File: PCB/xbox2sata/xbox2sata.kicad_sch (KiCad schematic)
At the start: 3 parts, among them U1 88SA8052

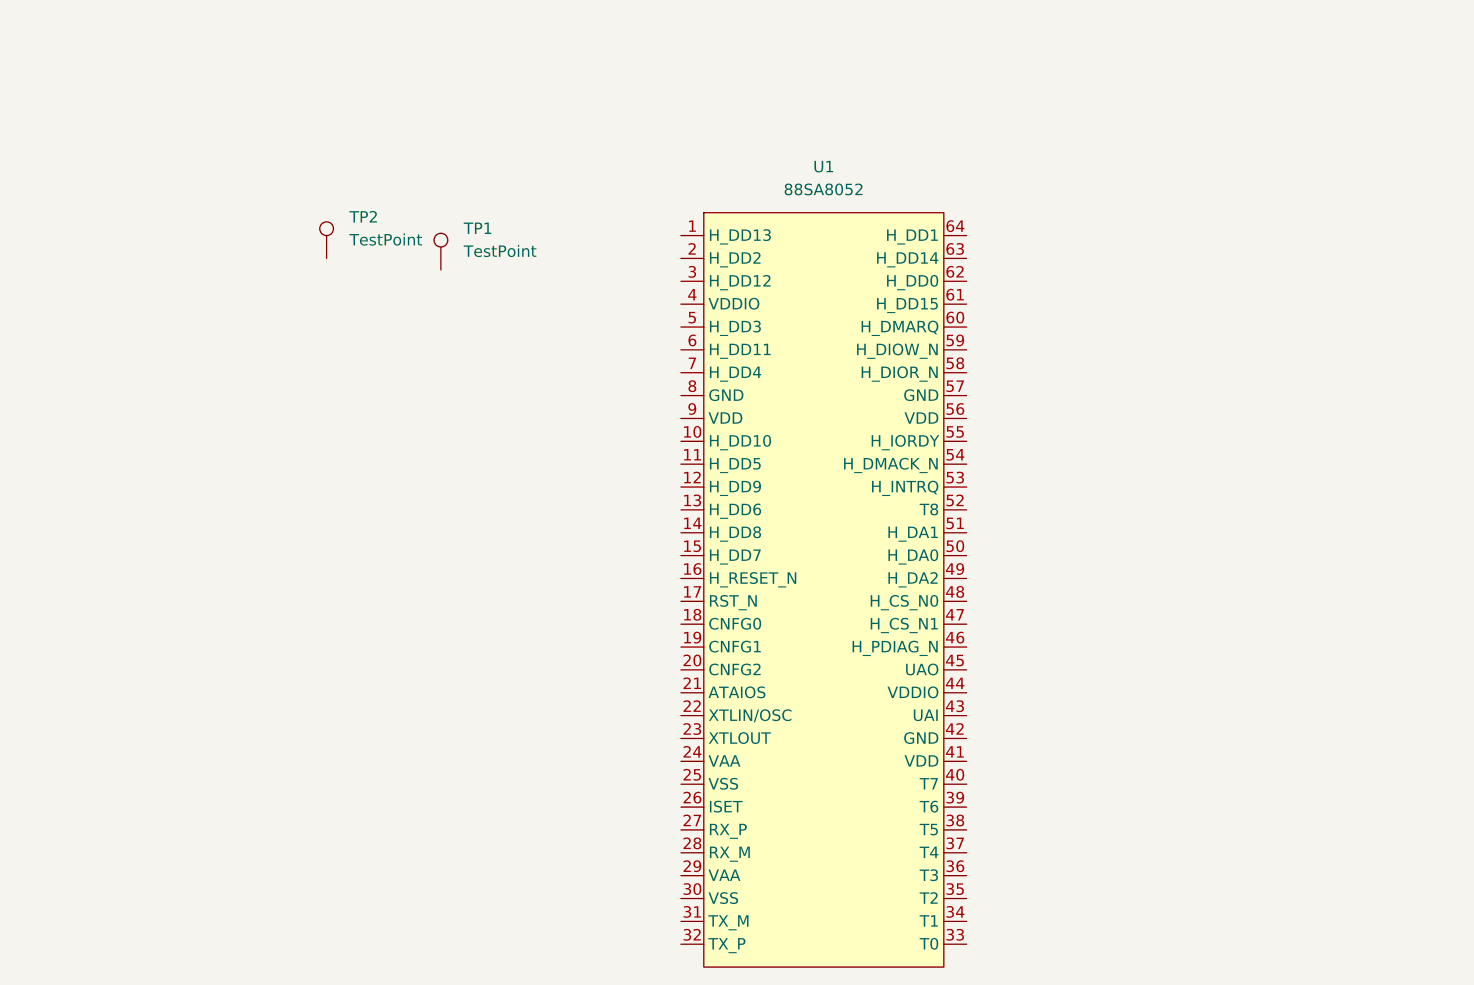
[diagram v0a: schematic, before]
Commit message: KIiCad symbols and footprints added
Added symbols, footprints, 3d models for Marvel 88SA, SATA data socket and IDE socket for DVD drive cable.

To try another 3d model for IDE socket.
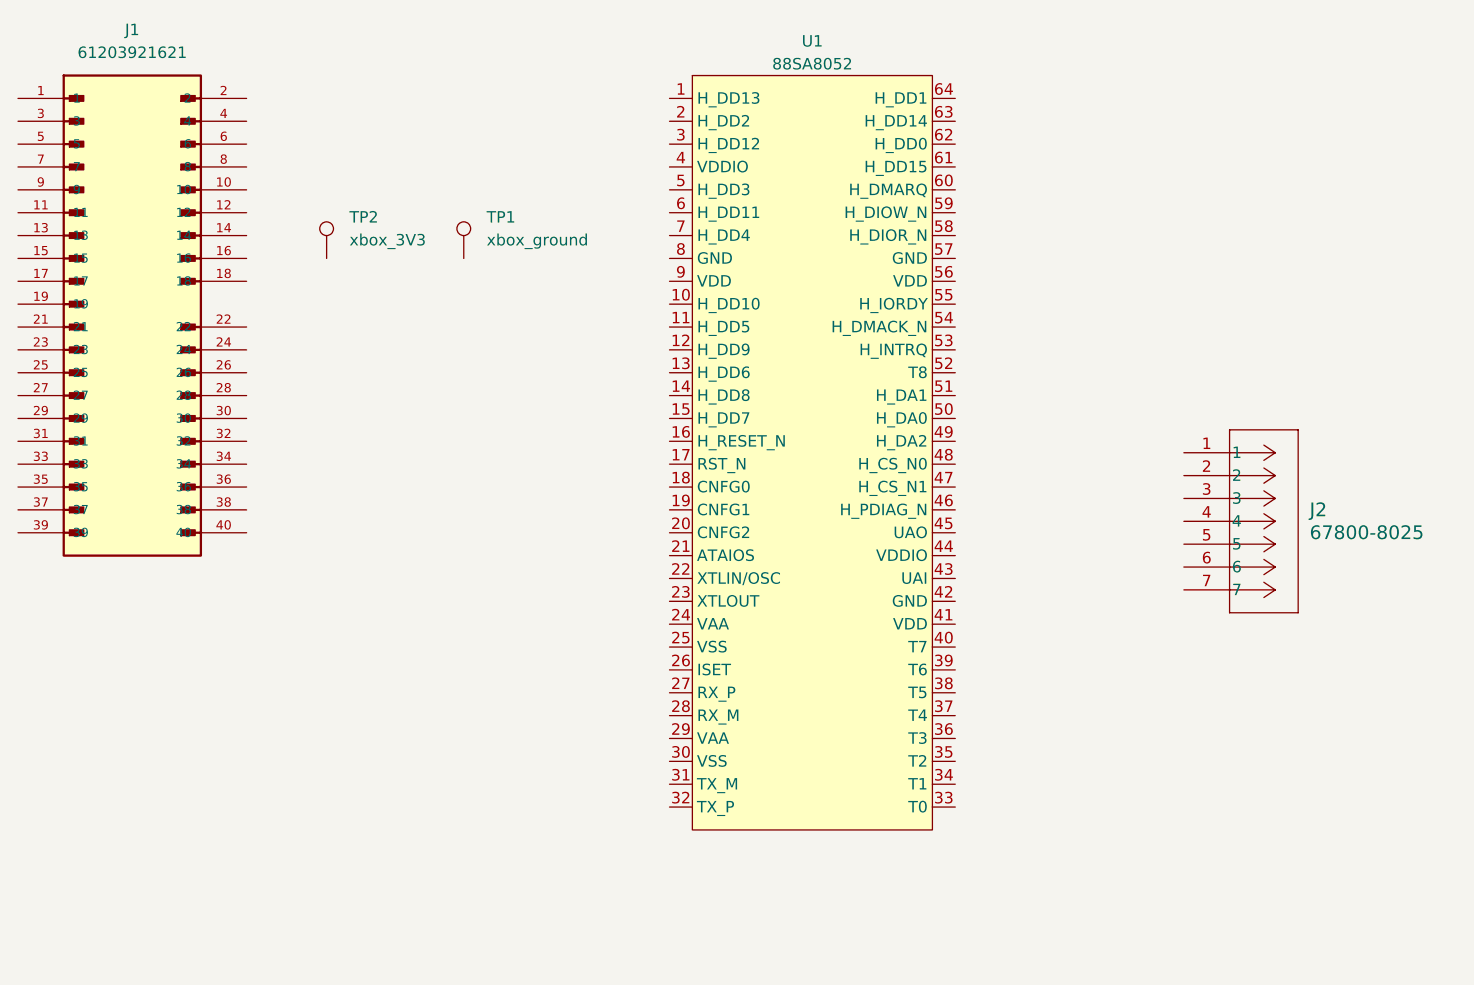
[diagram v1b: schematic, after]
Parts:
- removed U1: 88SA8052, Package_DFN_QFN:QFN-64-1EP_9x9mm_P0.5mm_EP3.4x3.4mm_ThermalVias, symbol Interface:88SA8052
- added J1: 61203921621, xbox2sata:WURTH-ELEKTRONIK_61203921621, symbol xbox2sata:61203921621
- added J2: 67800-8025, xbox2sata:CONN_67800-8025_MOL, symbol xbox2sata:67800-8025
- added U1: 88SA8052, Package_DFN_QFN:QFN-64-1EP_9x9mm_P0.5mm_EP3.4x3.4mm_ThermalVias, symbol xbox2sata:88SA8052
- TP1: value TestPoint -> xbox_ground
- TP2: value TestPoint -> xbox_3V3
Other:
- moved on the sheet: TP1

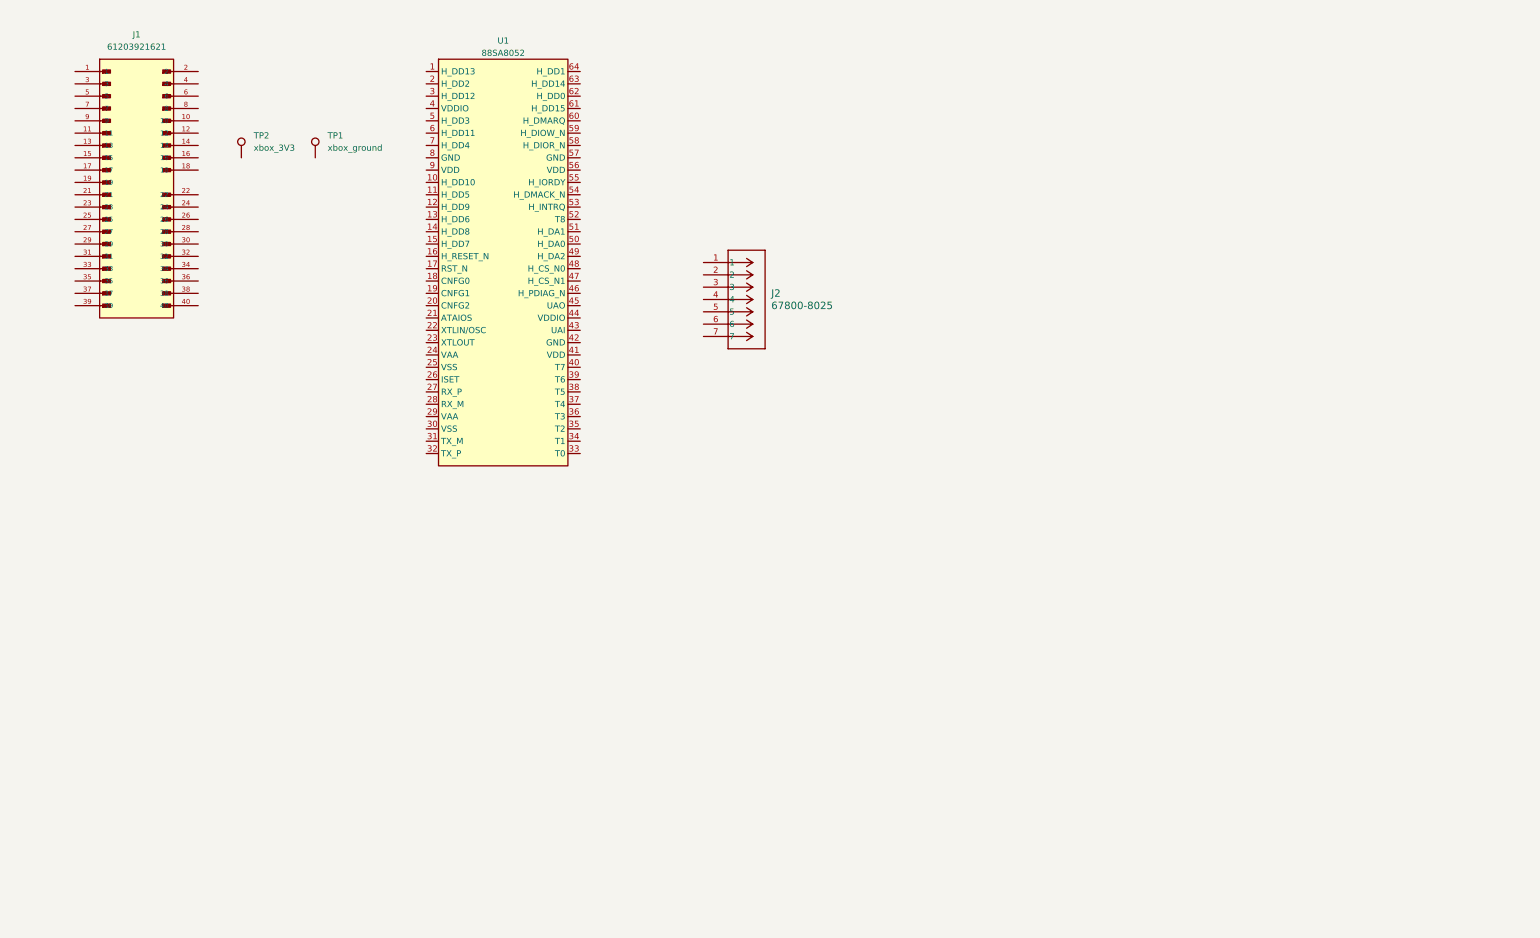
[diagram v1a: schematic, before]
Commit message: KiCad updates
Crystal resonator added, 3d model for ide header fixed.
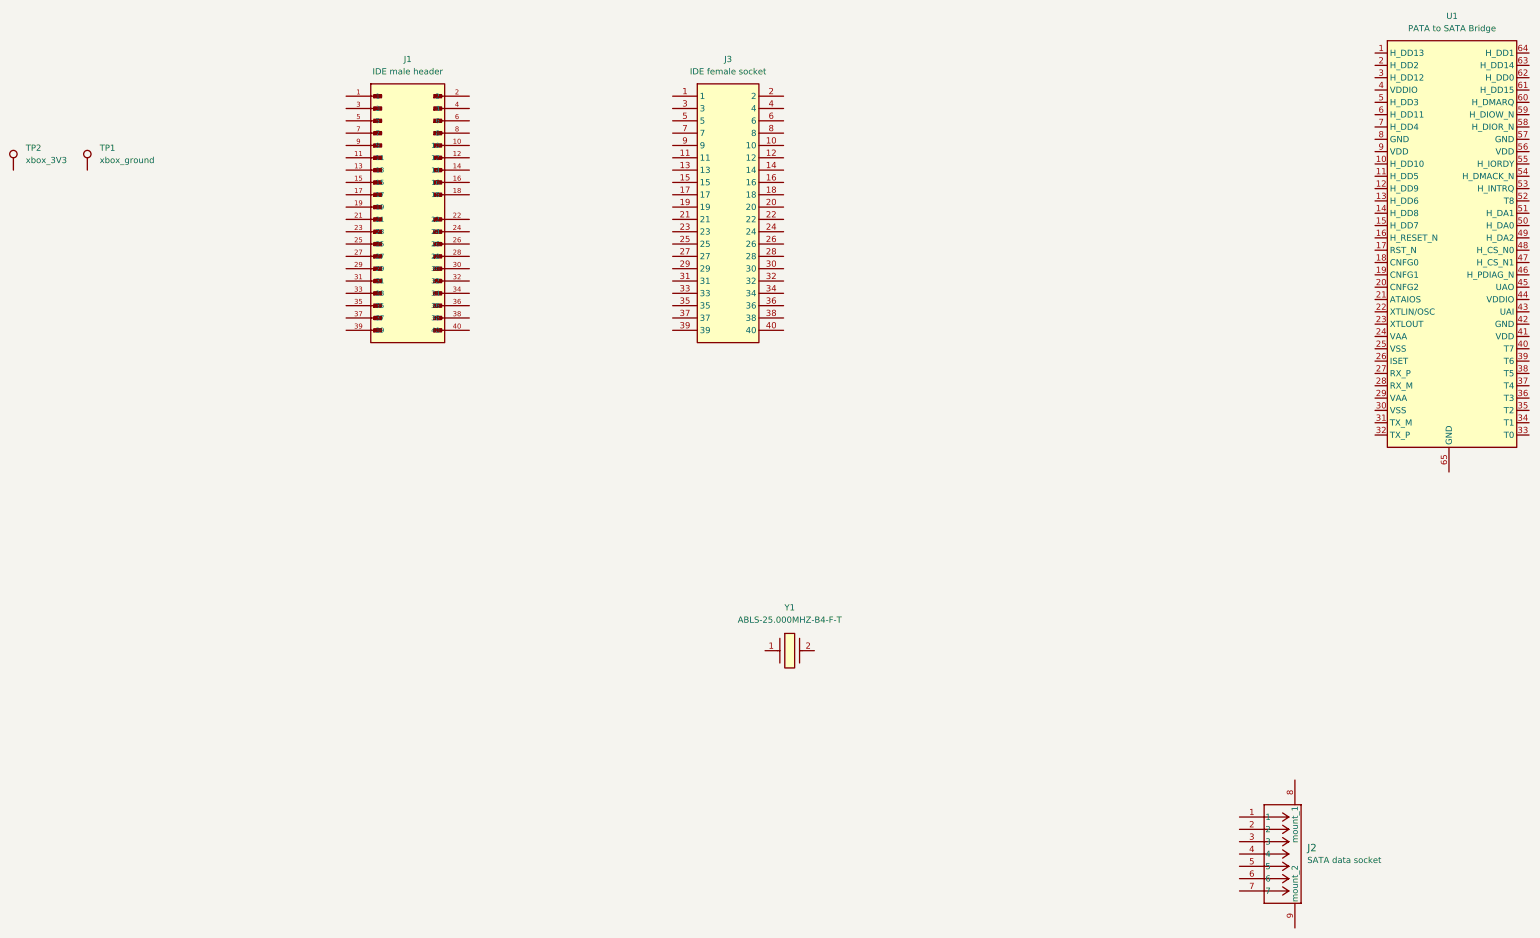
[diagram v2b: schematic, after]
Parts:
- added J3: 90151-2140, xbox2sata:RHDR40W70P254_2X20_5065X498X870P, symbol xbox2sata:90151-2140
- added Y1: ABLS-25.000MHZ-B4-F-T, xbox2sata:Crystal, symbol xbox2sata:ABLS-25.000MHZ-B4-F-T
- J1: footprint xbox2sata:WURTH-ELEKTRONIK_61203921621 -> 61203921621:WURTH-ELEKTRONIK_61203921621
- TP1, TP2: footprint (none) -> TestPoint:TestPoint_THTPad_2.5x2.5mm_Drill1.2mm
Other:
- moved on the sheet: TP1, TP2
